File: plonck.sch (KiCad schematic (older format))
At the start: 132 parts, among them J1 Battery_connector, J2 SWD, Q1 Q_PMOS_GSD, SW1 SW_Push, U1 SRV05-4, U2 TP4054-42-SOT25-R, U3 XC6206PxxxMR-Regulator_Linear, U4 nRF52840_holyiot_18010, q1 USB4085-GF-A_REVA

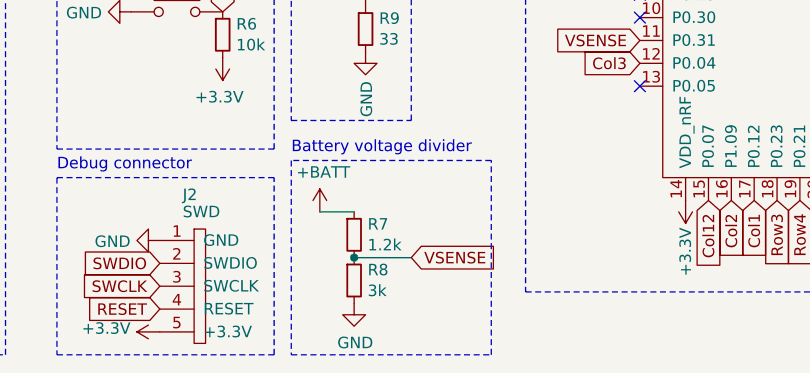
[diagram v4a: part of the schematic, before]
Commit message: updated resistor values for vsense
https://devzone.nordicsemi.com/nordic/nordic-blog/b/blog/posts/measuring-lithium-battery-voltage-with-nrf52
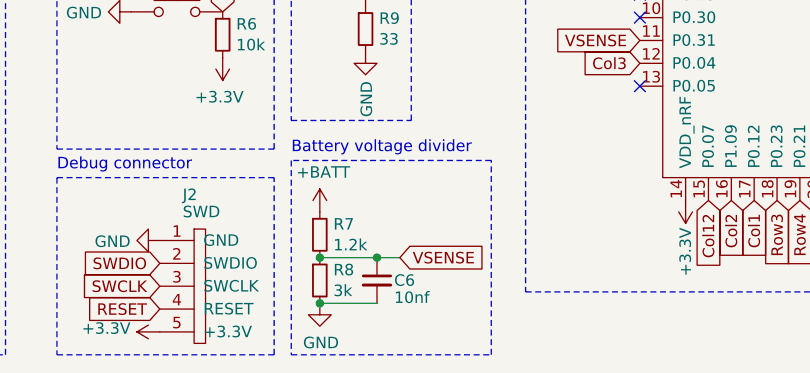
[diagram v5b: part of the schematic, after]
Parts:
- added C6: 10nf, Capacitor_SMD:C_0603_1608Metric, symbol Device:C_Small
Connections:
- net GND: now also C6.2
- net VSENSE: now also C6.1
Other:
- moved on the sheet: R7, R8
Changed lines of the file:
@@
 L Device:R_Small R7
 U 1 1 60C2226C
-P 3675 6925
-F 0 "R7" H 3734 6971 50  0000 L CNN
-F 1 "1.2k" H 3734 6880 50  0000 L CNN
-F 2 "Resistor_SMD:R_0603_1608Metric" H 3675 6925 50  0001 C CNN
-F 3 "https://datasheet.lcsc.com/lcsc/1811021221_UNI-ROYAL-Uniroyal-Elec-0603WAF1201T5E_C22765.pdf" H 3675 6925 50  0001 C CNN
-F 4 "C22765" H 3675 6925 50  0001 C CNN "LCSC"
-	1    3675 6925
+P 3525 6925
+F 0 "R7" H 3584 6971 50  0000 L CNN
+F 1 "1.2k" H 3584 6880 50  0000 L CNN
+F 2 "Resistor_SMD:R_0603_1608Metric" H 3525 6925 50  0001 C CNN
+F 3 "https://datasheet.lcsc.com/lcsc/1811021221_UNI-ROYAL-Uniroyal-Elec-0603WAF1201T5E_C22765.pdf" H 3525 6925 50  0001 C CNN
+F 4 "C22765" H 3525 6925 50  0001 C CNN "LCSC"
+	1    3525 6925
 	1    0    0    -1
 $EndComp
@@
 L Device:R_Small R8
 U 1 1 60C23717
-P 3675 7125
-F 0 "R8" H 3734 7171 50  0000 L CNN
-F 1 "3k" H 3734 7080 50  0000 L CNN
-F 2 "Resistor_SMD:R_0603_1608Metric" H 3675 7125 50  0001 C CNN
-F 3 "https://datasheet.lcsc.com/lcsc/1811131122_UNI-ROYAL-Uniroyal-Elec-0805W8F3001T5E_C17661.pdf" H 3675 7125 50  0001 C CNN
-F 4 "C17661" H 3675 7125 50  0001 C CNN "LCSC"
-	1    3675 7125
+P 3525 7125
+F 0 "R8" H 3584 7171 50  0000 L CNN
+F 1 "3k" H 3584 7080 50  0000 L CNN
+F 2 "Resistor_SMD:R_0603_1608Metric" H 3525 7125 50  0001 C CNN
+F 3 "https://datasheet.lcsc.com/lcsc/1811131122_UNI-ROYAL-Uniroyal-Elec-0805W8F3001T5E_C17661.pdf" H 3525 7125 50  0001 C CNN
+F 4 "C17661" H 3525 7125 50  0001 C CNN "LCSC"
+	1    3525 7125
 	1    0    0    -1
 $EndComp
@@
 L power:GND #PWR0102
 U 1 1 60C25DD1
-P 3675 7225
-F 0 "#PWR0102" H 3675 6975 50  0001 C CNN
-F 1 "GND" H 3680 7052 50  0000 C CNN
-F 2 "" H 3675 7225 50  0001 C CNN
-F 3 "" H 3675 7225 50  0001 C CNN
-	1    3675 7225
+P 3525 7225
+F 0 "#PWR0102" H 3525 6975 50  0001 C CNN
+F 1 "GND" H 3530 7052 50  0000 C CNN
+F 2 "" H 3525 7225 50  0001 C CNN
+F 3 "" H 3525 7225 50  0001 C CNN
+	1    3525 7225
 	1    0    0    -1
 $EndComp
 Wire Wire Line
-	3525 6825 3675 6825
-Wire Wire Line
-	3675 7025 3925 7025
-Connection ~ 3675 7025
-Text GLabel 3925 7025 2    50   Input ~ 0
+	3525 7025 3775 7025
+Connection ~ 3525 7025
+Text GLabel 3875 7025 2    50   Input ~ 0
 VSENSE
 Wire Notes Line
@@
 Wire Notes Line
 	3400 7450 4275 7450
-Wire Notes Line
-	4275 7450 4275 6600
 Wire Notes Line
 	4275 6600 3400 6600
@@
 Text GLabel 4925 5375 0    50   Input ~ 0
 BL_Led
+$Comp
+L Device:C_Small C6
+U 1 1 60BF820A
+P 3775 7125
+F 0 "C6" H 3850 7125 50  0000 L CNN
+F 1 "10nf" H 3850 7050 50  0000 L CNN
+F 2 "Capacitor_SMD:C_0603_1608Metric" H 3775 7125 50  0001 C CNN
+F 3 "~" H 3775 7125 50  0001 C CNN
+	1    3775 7125
+	1    0    0    -1
+$EndComp
+Connection ~ 3775 7025
+Wire Wire Line
+	3775 7025 3875 7025
+Wire Wire Line
+	3775 7225 3525 7225
+Connection ~ 3525 7225
+Wire Notes Line
+	4275 7450 4275 6600
 $EndSCHEMATC

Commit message: changed battery connector to smaller size
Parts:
- J1: footprint Connector_JST:JST_EH_S2B-EH_1x02_P2.50mm_Horizontal -> SM02B-SRSS-TB_LF__SN_:SM02B-SRSS-TB(LF)(SN)
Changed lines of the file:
@@
 F 0 "J1" H 7875 3425 50  0000 L CNN
 F 1 "Battery_connector" H 7875 3350 50  0000 L CNN
-F 2 "Connector_JST:JST_EH_S2B-EH_1x02_P2.50mm_Horizontal" H 7875 3450 50  0001 C CNN
+F 2 "SM02B-SRSS-TB_LF__SN_:SM02B-SRSS-TB(LF)(SN)" H 7875 3450 50  0001 C CNN
 F 3 "" H 7875 3450 50  0001 C CNN
 F 4 "" H 7875 3450 50  0001 C CNN "LCSC"
